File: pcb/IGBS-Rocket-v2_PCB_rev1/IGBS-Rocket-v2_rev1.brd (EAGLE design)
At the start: 182.9 x 34.9 mm, 250 parts, among them IC1 NCV21872DR2G, IC2 NCV21872DR2G, IC3 NCV21872DR2G, Q1 BC817, Q2 ENC-03, Q3 BSS316N, Q4 BC817, Q5 BSS314PE, U1 STM32H750VBT6, U2 LM317BD2TG, U3 CS5171EDR8G, U5 MICROSD, U6 ESP-12E/F, U8 LP324DRG4, U9 MCP6V51T-E/MS, Y1 24MHz

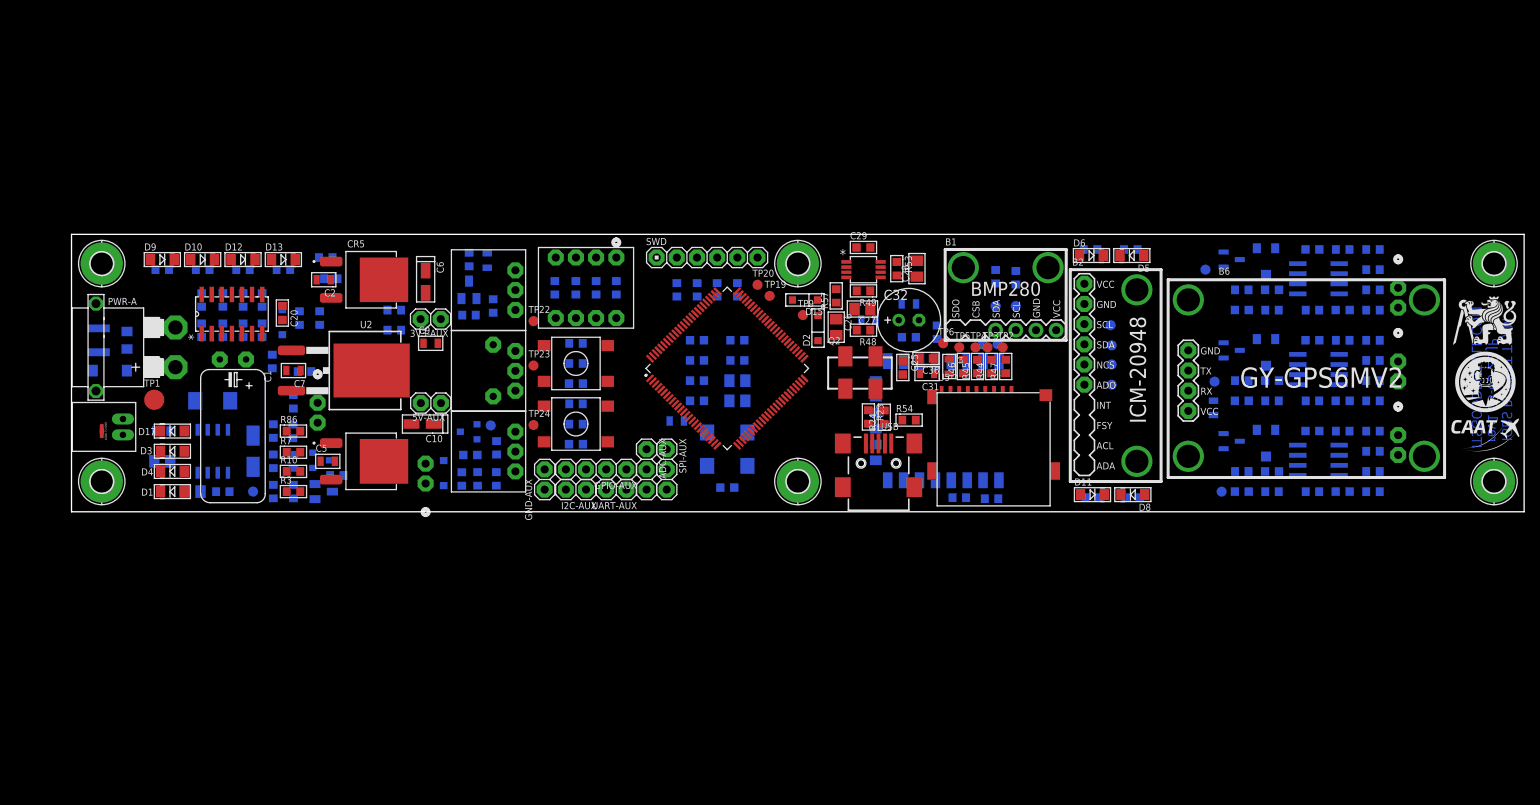
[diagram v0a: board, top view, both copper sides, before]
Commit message: * PCB schematics upgrade (removed all modules) last thing GPS part needs to be done
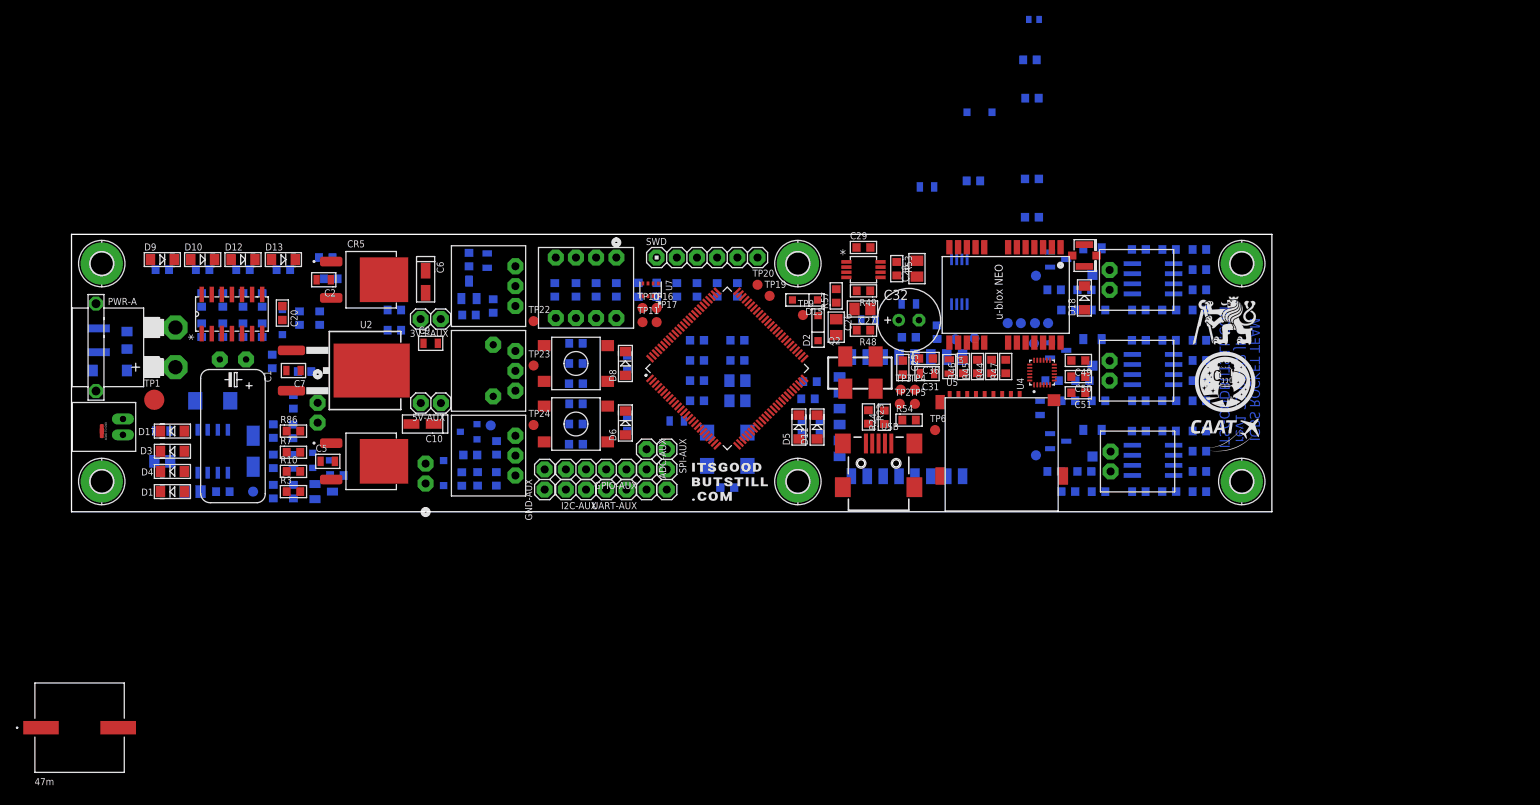
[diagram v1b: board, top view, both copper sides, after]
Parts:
- removed B1: BMP280, modules:BMP280-LESSPINS
- removed B2: ICM-20948, modules:ICM-20948-LESSPINS
- removed B6: GY-NEO6MV2, modules:GY-NEO6MV2
- added C48, C49, C50, C51, C52, C53, C54: 100n, rcl2:C0603K
- added C55: 10u, SparkFun-Capacitors:0805-CAP
- added C56: 47m, supercap:FC0H473ZFTBR24_KEM
- added D18: GREEN, leds:LED-1206
- added D19: 1N4148, SparkFun-DiscreteSemi:SOD-123
- added J1: U.FL, SparkFun-Connectors:U.FL
- added L6: 27nH, rcl2:C0402
- added R99: 1k, rcl2:R0603
- added TP16, TP17: TPB1,27, testpad2:B1,27
- added U$2: u-blox NEO-M6, gps:NEO-M8
- added U10: 24AA32A-I/ST, eeprom:TSSOP8_MC_MCH
- added U4: MPU-9250, gyro:QFN40P300X300X105-24N
- added U7: BMP280, gyro:XDCR_BMP280
- R55: value 4k7 -> 10R
- R56: value 4k7 -> 1k
- moved D8 66.0 mm to (69.7, 18.7), turned to 90 degrees
- moved R25 65.9 mm to (70.0, 18.8), turned to 90 degrees
- moved D6 62.3 mm to (69.7, 11.2), turned to 90 degrees
- moved R20 62.3 mm to (70.0, 11.0), turned to 90 degrees
- moved D5 47.1 mm to (91.6, 10.7), turned to 90 degrees
- moved R19 47.1 mm to (91.9, 10.7), turned to 90 degrees
- moved TP11 47.0 mm to (71.9, 23.9), flipped to the top
- moved TP10 44.5 mm to (71.9, 25.7), flipped to the top
- moved SG3 36.5 mm to (130.8, 5.08), flipped to the top, turned to 90 degrees
- moved SG2 36.4 mm to (130.7, 16.5), flipped to the top, turned to 90 degrees
- moved SG1 36.3 mm to (130.7, 27.9), flipped to the top, turned to 90 degrees
- moved D11 35.7 mm to (93.9, 10.7), turned to 90 degrees
- moved R21 35.4 mm to (94.2, 10.7), turned to 90 degrees
- moved H1 31.8 mm to (147.3, 31.2)
- moved H2 31.8 mm to (147.3, 3.81)
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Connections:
- removed net MAIN-SCL: B1.4, R55.1, TP11.TP, U1.92
- removed net MAIN-SDA: B1.3, R56.1, TP10.TP, U1.93
- new net BMP-CS: TP17.TP, U1.3, U7.2
- new net BMP-MISO: TP10.TP, U1.4, U7.5
- new net BMP-MOSI: TP16.TP, U1.5, U7.3
- new net BMP-SCK: TP11.TP, U1.1, U7.4
- new net N$74: C51.2, U4.10
- net 3V3: now also C48.2, C49.2, C50.2, C52.2, U4.13, U4.8, U7.6, U7.8; no longer B1.6, B2.1, B6.4, R55.2, R56.2
- net BUZZER: now also U1.63; no longer U1.5
- net CTRL-12V: now also U1.98; no longer U1.7
- net GND: now also C48.1, C49.1, C50.1, C51.1, C52.1, U4.1, U4.18, U4.19, U4.20, U7.1, U7.7; no longer B1.5, B1.HOLE1, B1.HOLE2, B2.2, B2.HOLE1, B2.HOLE2, B6.1, B6.HOLE1, B6.HOLE2, B6.HOLE3, B6.HOLE4
- net GPIO-AUX-IN1: now also U1.2; no longer U1.1
- net GPIO-AUX-IN2: now also U1.7; no longer U1.2
- net GPIO-AUX-OUT1: now also U1.8; no longer U1.3
- net GPIO-AUX-OUT2: now also U1.9; no longer U1.4
- net GPS-RX: no longer B6.3
- net GPS-TX: no longer B6.2
- net ICM-CS: now also U4.22; no longer B2.5
- net ICM-MISO: now also U4.9; no longer B2.6
- net ICM-MOSI: now also U4.24; no longer B2.4
- net ICM-SCK: now also U4.23; no longer B2.3
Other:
- board size 182.9 x 34.9 mm -> 151.1 x 34.9 mm

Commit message: + PCB layout DONE + PCB 3D model is ready
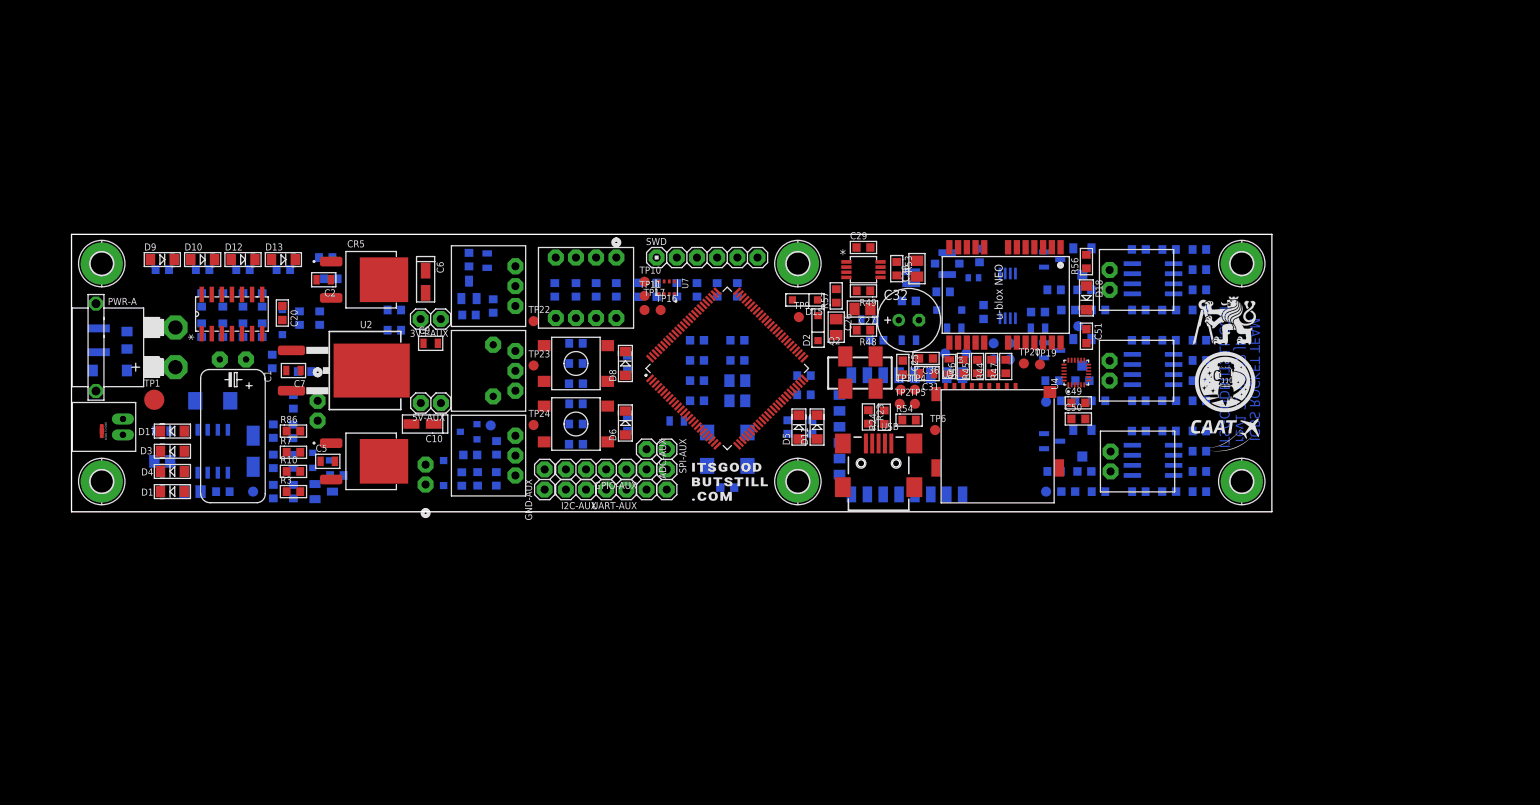
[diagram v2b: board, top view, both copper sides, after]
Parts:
- removed C56: 47m, supercap:FC0H473ZFTBR24_KEM
- added BT1: MS621FE-3V, SparkFun-Batteries:BATTCON-6.8MM
- 3V3-AUX, 5V-AUX, GND-AUX, I2C-AUX, UART-AUX: device pinhead2:1X02 -> pinhead2-nopin:1X02
- ADC-AUX, SPI-AUX: device pinhead2:1X03 -> pinhead2-nopin:1X03
- GPIO-AUX: device pinhead2:1X04 -> pinhead2-nopin:1X04
- moved TP19 35.1 mm to (121.9, 18.5)
- moved TP20 35.0 mm to (119.9, 18.7)
- moved L6 33.4 mm to (113.5, 29.5), turned to 180 degrees
- moved R55 25.4 mm to (114.3, 32.3), turned to 90 degrees
- moved D19 25.2 mm to (110.5, 25.4), turned to 180 degrees
- moved C55 22.6 mm to (121.7, 23.1)
- moved R56 21.7 mm to (127.8, 31.5), flipped to the top, turned to 90 degrees
- moved J1 17.3 mm to (110.2, 31.2), flipped to the bottom, turned to 180 degrees
- moved C53 16.8 mm to (121.7, 25.1)
- moved L3 14.7 mm to (111.1, 23.1), turned to 0 degrees
- moved R99 14.5 mm to (109.7, 27.7), turned to 180 degrees
- moved C54 13.4 mm to (114.8, 25.1), turned to 90 degrees
- moved TP26 8.29 mm to (126.7, 23.4)
- moved R52 7.69 mm to (101.3, 21.6), turned to 180 degrees
- moved TP27 7.52 mm to (122.7, 13.8)
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- renumbered U$2 to U11
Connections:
- new net GPS-RF-IN: J1.P$3, L6.1, U11.11
- new net GPS-VBCKP: BT1.+, R99.2, U11.22
- new net GPS-VCC: C53.1, C55.1, D19.A, L3.1, U11.23
- new net GPS-VCC-RF: R55.2, U11.8, U11.9
- new net N$69: U10.6, U11.19
- new net N$73: U10.5, U11.18
- new net N$76: D19.C, R99.1
- new net N$78: D18.A, R56.1
- new net N$79: L6.2, R55.1
- new net N$80: R56.2, U11.3
- net GND: now also BT1.-, C53.2, C54.2, C55.2, D18.C, J1.P$1, J1.P$2, U10.1, U10.2, U10.3, U10.4, U10.7, U11.10, U11.12, U11.13, U11.24
- net GPS-RX: now also U11.21
- net GPS-TX: now also U11.20
- net VCC: now also C54.1, U10.8; no longer L3.1

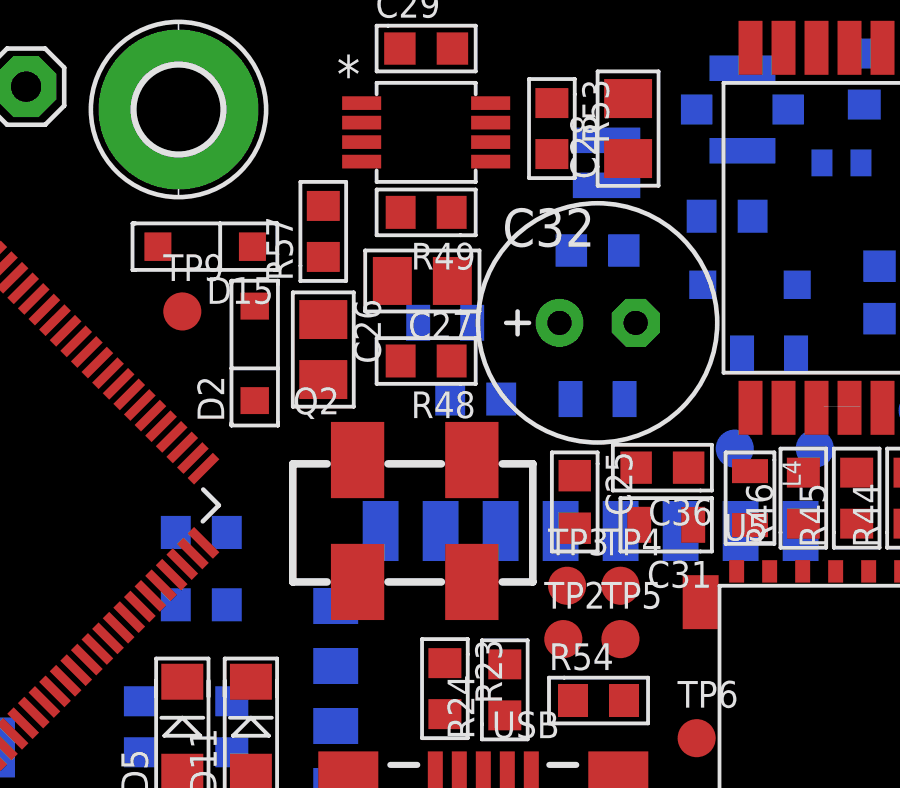
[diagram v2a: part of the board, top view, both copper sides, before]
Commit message: * 3D model of hole minor fix
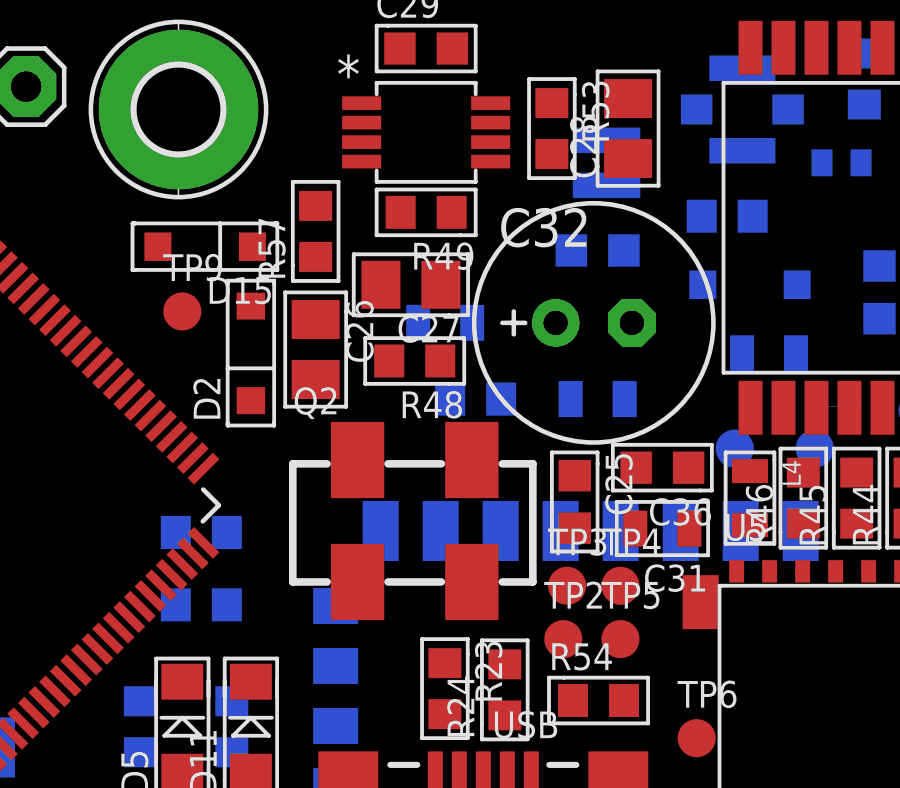
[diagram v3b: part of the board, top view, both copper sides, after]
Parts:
- moved C27 0.40 mm to (99.2, 25.4)
- moved R48 0.38 mm to (99.3, 22.9)
- moved C26 0.25 mm to (96.0, 23.2)
- moved R57 0.25 mm to (96.0, 27.2)
- moved C31 0.18 mm to (107.6, 17.3)
- moved D2 0.13 mm to (93.9, 23.1)
- moved C32 0.13 mm to (105.3, 24.1)

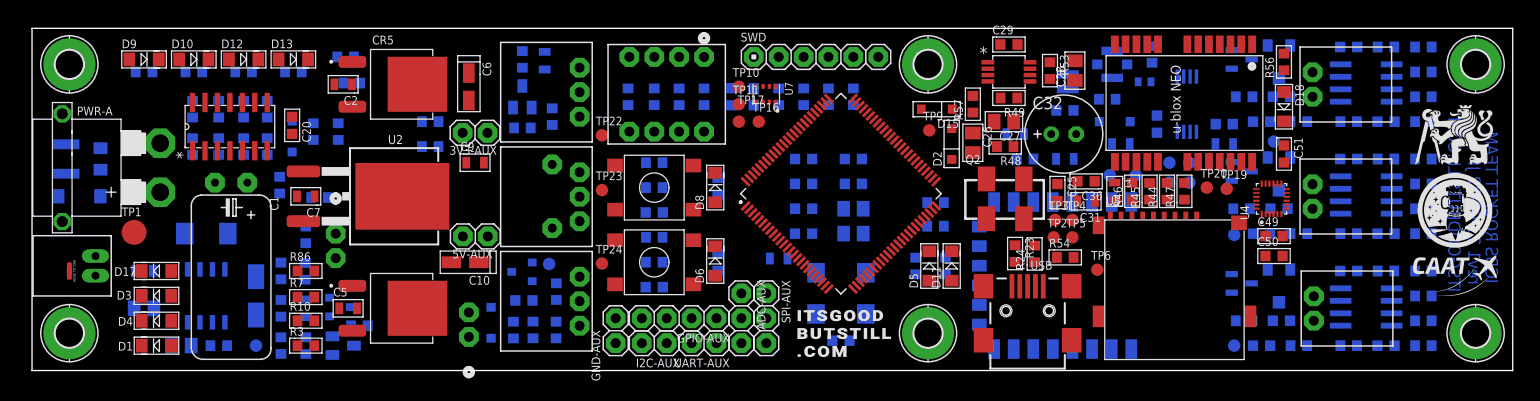
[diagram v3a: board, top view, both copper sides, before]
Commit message: + PCB layout checking and cleaning up (silkscreen)
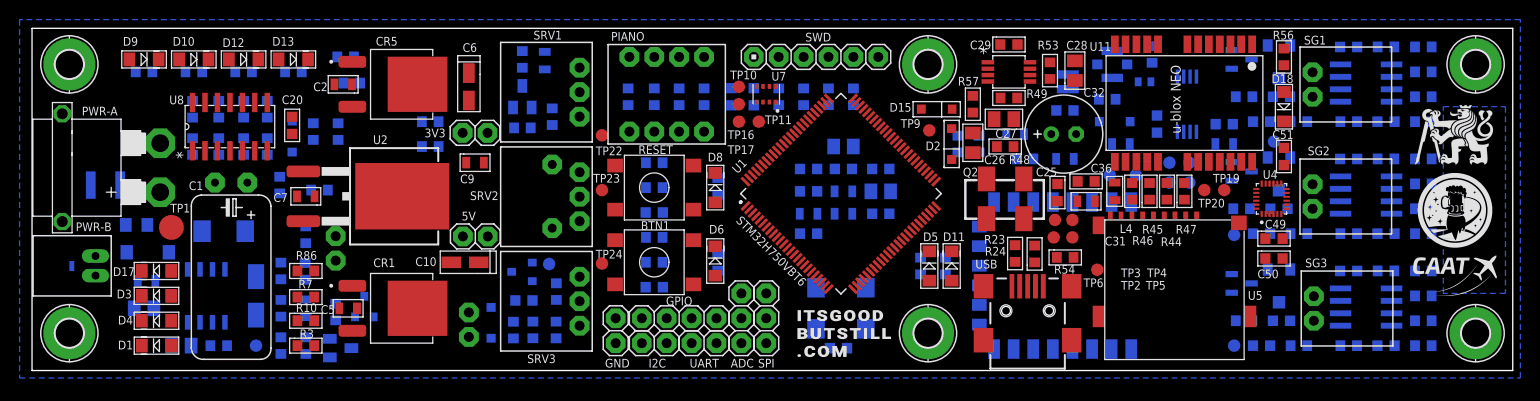
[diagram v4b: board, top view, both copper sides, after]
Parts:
- added C56, C57: 10u, SparkFun-Capacitors:0805-CAP
- moved C13 10.3 mm to (86.6, 20.6), turned to 0 degrees
- moved D7 9.03 mm to (11.8, 12.1), turned to 180 degrees
- moved C17 8.95 mm to (82.8, 22.9)
- moved C15 8.89 mm to (79.2, 14.0)
- moved R51 8.69 mm to (94.5, 23.1), turned to 90 degrees
- moved C12 8.44 mm to (86.6, 16.0), turned to 0 degrees
- moved MOV1 7.67 mm to (10.7, 14.9), turned to 0 degrees
- moved R50 7.44 mm to (96.6, 23.1), turned to 90 degrees
- moved L1 5.49 mm to (79.2, 16.0)
- moved PPTC1 4.86 mm to (7.49, 18.9), turned to 180 degrees
- moved TP1 3.84 mm to (14.2, 14.6)
- moved C16 3.31 mm to (86.6, 18.3)
- moved R97 2.79 mm to (31.0, 5.97), turned to 270 degrees
- moved Q5 2.54 mm to (33.9, 6.48), turned to 0 degrees
- moved C14 1.85 mm to (79.2, 18.3), turned to 0 degrees
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- renumbered 3V3-AUX to 3V3, 5V-AUX to 5V, ADC-AUX to ADC, GND-AUX to GND, GPIO-AUX to GPIO, I2C-AUX to I2C, SPI-AUX to SPI, UART-AUX to UART
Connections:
- removed net N$3: C15.2, L1.1, U1.20, U1.21
- new net VDDA: C15.2, C56.1, L1.1, U1.20, U1.21
- net 3V3: now also C57.1
- net GND: now also C56.2, C57.2
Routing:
- added copper zone on layer 16, net GND
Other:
- board text added: "rev1 23-03-22 JP."
- board text removed: "rev1 23-03-22 JP"
